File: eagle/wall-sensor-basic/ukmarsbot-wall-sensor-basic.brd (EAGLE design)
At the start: 81.3 x 27.9 mm, 22 parts, among them Q1 2N2222*, T1 BPW96B, T2 BPW96B, T3 BPW96B

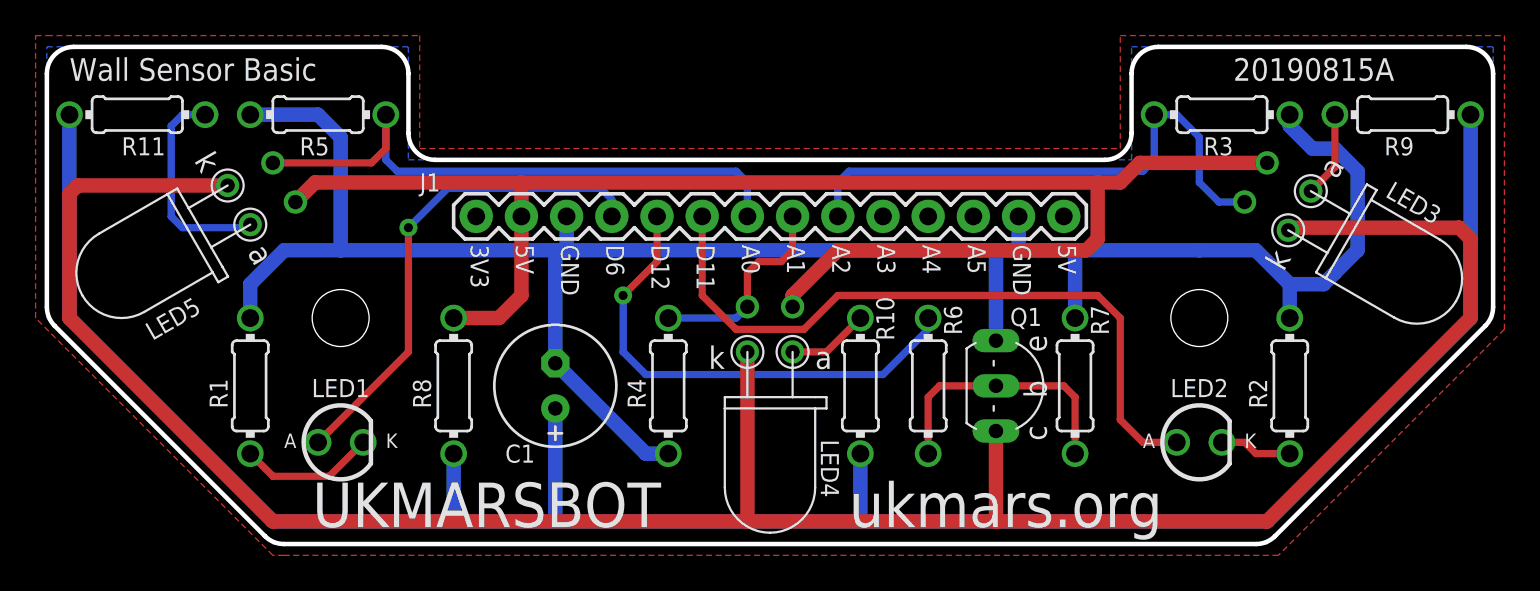
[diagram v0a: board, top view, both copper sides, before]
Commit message: Update Basic Wall Sensor board and library with larger pads/holes
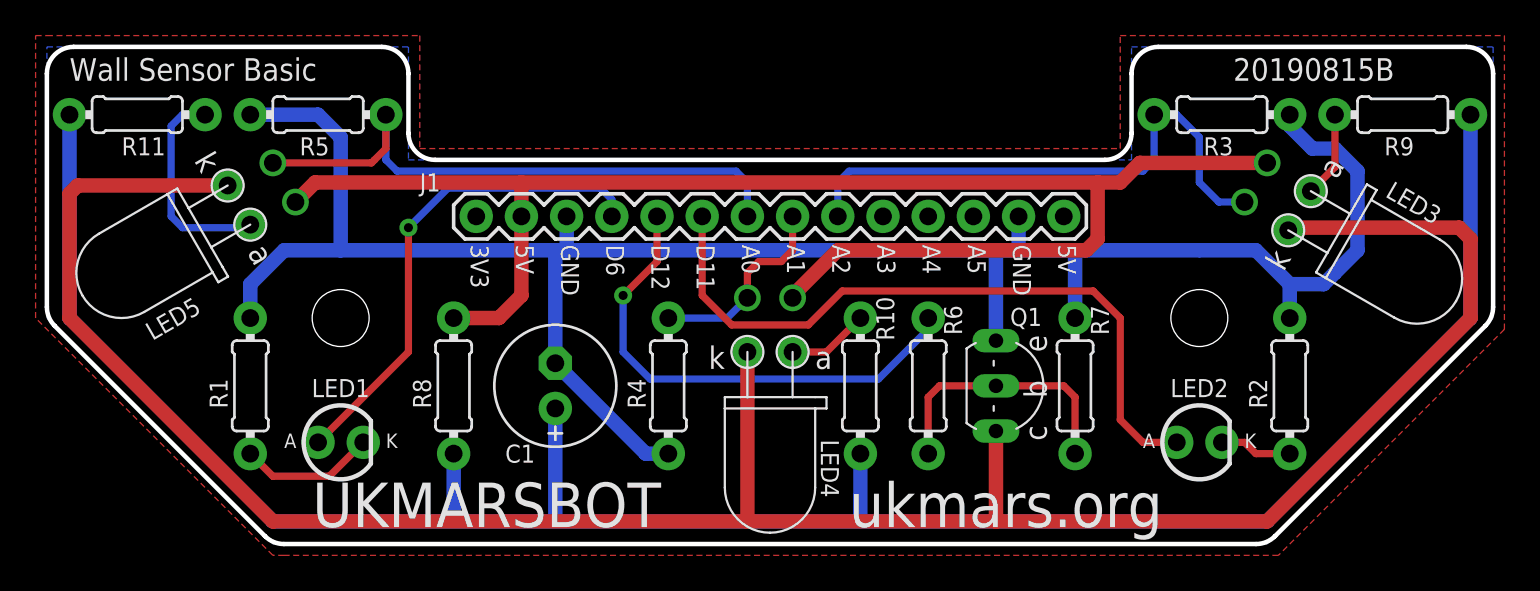
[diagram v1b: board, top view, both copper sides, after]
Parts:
- Q1: value 2N2222* -> BC337*
- moved T2 0.50 mm to (49.5, 64.6)
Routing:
- net 5V: track 88.5 -> 88.0 mm
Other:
- board text added: "20190815B"
- board text removed: "20190815A"

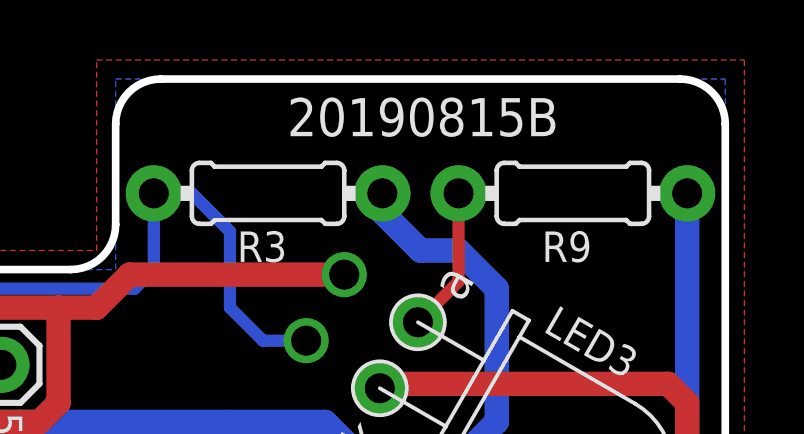
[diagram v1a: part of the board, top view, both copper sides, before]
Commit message: Remove deprecated SFH4550 references
Board 20190815C has generic emitters in schematic and on the silk screen.
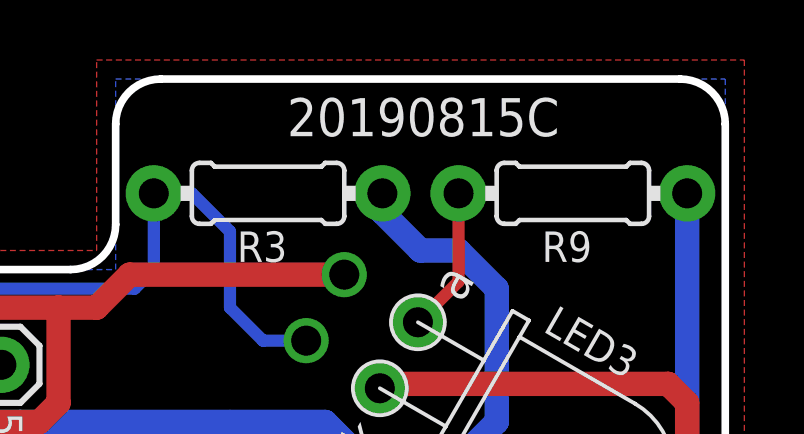
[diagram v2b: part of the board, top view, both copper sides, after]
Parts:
- LED3, LED4, LED5: value SFH4550 -> Emitter
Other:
- board text added: "20190815C"
- board text removed: "20190815B"
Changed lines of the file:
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@@
 <?xml version="1.0" encoding="utf-8"?>
 <!DOCTYPE eagle SYSTEM "eagle.dtd">
-<eagle version="7.6.0">
+<eagle version="7.5.0">
 <drawing>
 <settings>
@@
 <text x="53.975" y="51.7525" size="2.5" layer="25" font="vector" ratio="17">ukmars.org</text>
 <text x="10.16" y="76.835" size="1.27" layer="25" font="vector" ratio="17">Wall Sensor Basic</text>
-<text x="75.565" y="76.835" size="1.27" layer="25" font="vector" ratio="17">20190815B</text>
+<text x="75.565" y="76.835" size="1.27" layer="25" font="vector" ratio="17">20190815C</text>
 </plain>
 <attributes>
@@
 <attribute name="VALUE" x="31.75" y="67.183" size="0.6096" layer="27" font="vector" ratio="20"/>
 </element>
-<element name="LED3" library="ukmarsbot" package="LED-5MM-SIDE" value="SFH4550" x="79.289925" y="69.5325" smashed="yes" rot="R240">
+<element name="LED3" library="ukmarsbot" package="LED-5MM-SIDE" value="Emitter" x="79.289925" y="69.5325" smashed="yes" rot="R240">
 <attribute name="NAME" x="84.056159375" y="70.347634375" size="1.016" layer="25" font="vector" ratio="17" rot="R330"/>
 <attribute name="VALUE" x="79.452409375" y="64.97293125" size="1.016" layer="27" font="vector" ratio="17" rot="R330"/>
 </element>
-<element name="LED4" library="ukmarsbot" package="LED-5MM-SIDE" value="SFH4550" x="49.53" y="61.595" smashed="yes" rot="R180">
+<element name="LED4" library="ukmarsbot" package="LED-5MM-SIDE" value="Emitter" x="49.53" y="61.595" smashed="yes" rot="R180">
 <attribute name="NAME" x="52.3875" y="56.67375" size="1.016" layer="25" font="vector" ratio="17" rot="SR270"/>
 <attribute name="VALUE" x="45.72" y="59.69" size="1.016" layer="27" font="vector" ratio="17" rot="R270"/>
 </element>
-<element name="LED5" library="ukmarsbot" package="LED-5MM-SIDE" value="SFH4550" x="19.685" y="69.85" smashed="yes" rot="R120">
+<element name="LED5" library="ukmarsbot" package="LED-5MM-SIDE" value="Emitter" x="19.685" y="69.85" smashed="yes" rot="R120">
 <attribute name="NAME" x="14.8200625" y="62.21543125" size="1.016" layer="25" font="vector" ratio="17" rot="R30"/>
 <attribute name="VALUE" x="16.32384375" y="72.63699375" size="1.016" layer="27" font="vector" ratio="17" rot="R210"/>
